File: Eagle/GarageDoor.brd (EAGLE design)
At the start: 27.4 x 31.8 mm, 30 parts, among them Q1 P-FET

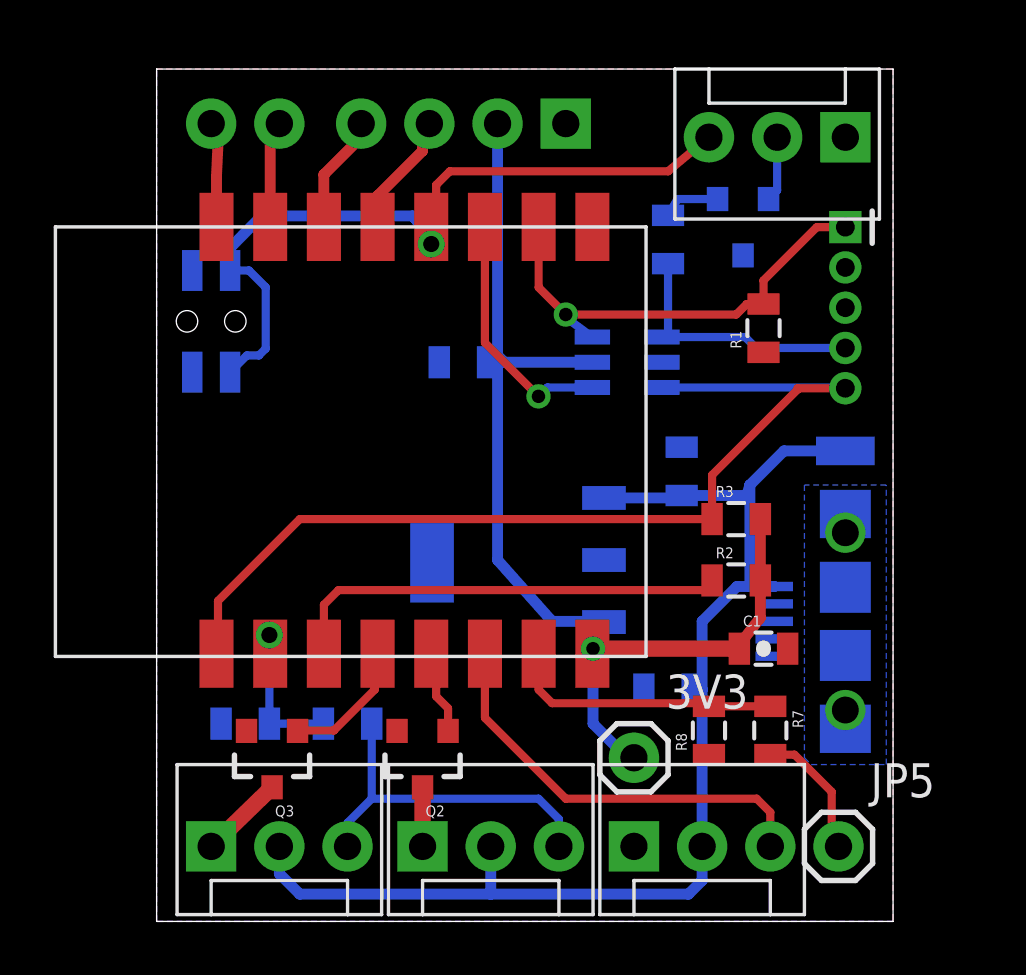
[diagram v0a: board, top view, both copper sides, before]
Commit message: Changed to positive side sensor control
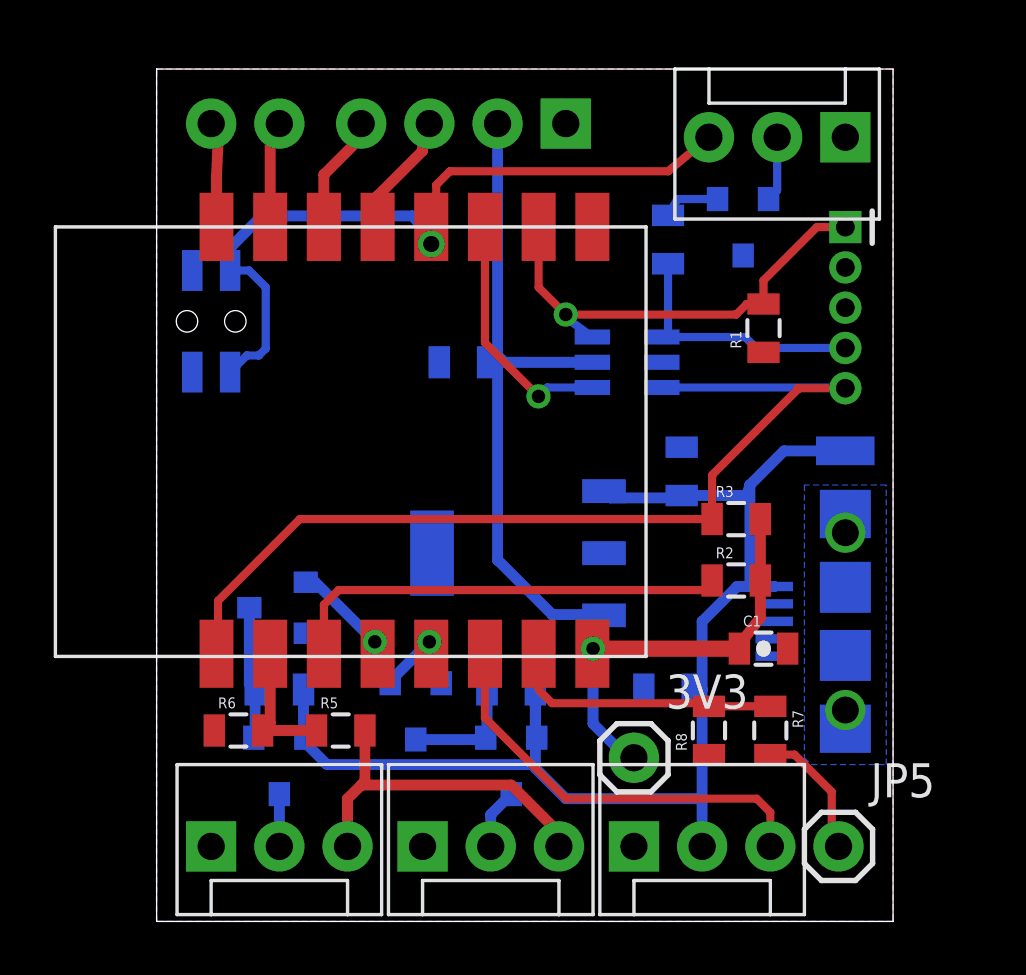
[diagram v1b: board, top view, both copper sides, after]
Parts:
- added Q4, Q5: P-FET, SparkFun-DiscreteSemi:SOT23-3
- added R10, R9: 10K, SparkFun-Resistors:0805
- moved Q3 5.59 mm to (4.55, 11.7), flipped to the bottom, turned to 270 degrees
- moved Q2 1.80 mm to (9.65, 7.87), flipped to the bottom
- moved R5 0.36 mm to (6.86, 7.11), flipped to the top, turned to 0 degrees
- moved R6 0.36 mm to (3.05, 7.11), flipped to the top, turned to 0 degrees
- moved 3V3R 0.25 mm to (13.5, 13.7)
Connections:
- new net N$12: Q2.3, Q5.1, R10.1
- new net N$13: JP3.2, Q5.3
- net +5V: now also Q4.2, Q5.2, R10.2, R9.2; no longer JP2.2, JP3.2
- net GND: now also JP2.1, JP3.1
- net N$2: now also JP2.2, Q4.3; no longer JP2.1, Q3.3
- net N$6: now also Q3.3, Q4.1, R9.1; no longer JP3.1, Q2.3
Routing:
- net N$12: track 0.00 -> 4.45 mm
- net N$6: track 2.20 -> 4.95 mm
- net N$13: track 0.00 -> 2.26 mm
- net +5V: track 46.8 -> 49.0 mm
- net IO16: track 5.64 -> 3.98 mm, vias 0 -> 1
- net N$2: track 3.16 -> 1.95 mm
- net ADC: track 6.13 -> 4.98 mm, vias 1 -> 0
- net 3V3: track 43.1 -> 42.1 mm
- net IO14: track 3.13 -> 2.69 mm, vias 0 -> 1

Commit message: Changed to NPN output
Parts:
- Q1: value P-FET -> (none)
- R10, R6, R9: value 10K -> 4K7
- R4: value 10K -> 1K
- R5: value 10K -> 5K6
- moved R4 0.76 mm to (19.1, 24.6)
- moved Q1 0.36 mm to (22.1, 25.7), turned to 90 degrees
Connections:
- net GND: now also Q1.2; no longer Q1.3
- net N$1: now also Q1.3; no longer Q1.2
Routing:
- net N$1: track 2.43 -> 3.59 mm
- net ICSPDAT: track 10.5 -> 9.89 mm
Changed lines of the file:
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@@
 <element name="." library="SparkFun-Connectors" package="1X02" value="" x="2.032" y="29.718" rot="MR180"/>
 <element name="C1" library="SparkFun-Capacitors" package="0805-CAP" value="0.1uF" x="22.606" y="10.16"/>
-<element name="Q1" library="SparkFun-DiscreteSemi" package="SOT23-3" value="P-FET" x="21.844" y="25.908" rot="MR180"/>
 <element name="U$3" library="CuriousTech" package="SMD-PAD1" value="SMD-PAD1" x="25.654" y="17.526" rot="MR180"/>
 <element name="10F320" library="Microchip_By_element14_Batch_1" package="SOT95P270X145-6N" value="PIC10F320T-I/OT" x="17.526" y="20.828" rot="MR0">
@@
 <element name="C4" library="SparkFun-Capacitors" package="0805-CAP" value="1uF" x="19.558" y="16.764" rot="MR90"/>
 <element name="JP4" library="SparkFun-Connectors" package="MOLEX-1X3" value="" x="17.78" y="2.794"/>
-<element name="R4" library="SparkFun-Resistors" package="0805" value="10K" x="19.05" y="25.4" rot="MR270"/>
+<element name="R4" library="SparkFun-Resistors" package="0805" value="1K" x="19.05" y="24.638" rot="MR270"/>
 <element name="C3" library="SparkFun-Capacitors" package="0805-CAP" value="0.1uF" x="19.05" y="8.636" rot="MR0"/>
-<element name="R5" library="SparkFun-Resistors" package="0805" value="10K" x="6.858" y="7.112"/>
-<element name="R6" library="SparkFun-Resistors" package="0805" value="10K" x="3.048" y="7.112"/>
+<element name="R5" library="SparkFun-Resistors" package="0805" value="5K6" x="6.858" y="7.112"/>
+<element name="R6" library="SparkFun-Resistors" package="0805" value="4K7" x="3.048" y="7.112"/>
 <element name="JP5" library="SparkFun-Connectors" package="1X01" value="" x="25.4" y="2.794"/>
 <element name="JP6" library="SparkFun-Connectors" package="MOLEX-1X3" value="" x="25.654" y="29.21" rot="R180"/>
@@
 <element name="3V3" library="SparkFun-Connectors" package="1X01" value="" x="17.78" y="6.096"/>
 <element name="Q4" library="SparkFun-DiscreteSemi" package="SOT23-3" value="P-FET" x="4.572" y="5.842" rot="MR180"/>
-<element name="R9" library="SparkFun-Resistors" package="0805" value="10K" x="4.572" y="8.636" rot="MR180"/>
+<element name="R9" library="SparkFun-Resistors" package="0805" value="4K7" x="4.572" y="8.636" rot="MR180"/>
 <element name="Q5" library="SparkFun-DiscreteSemi" package="SOT23-3" value="P-FET" x="13.208" y="5.842" rot="MR180"/>
-<element name="R10" library="SparkFun-Resistors" package="0805" value="10K" x="13.208" y="8.636" rot="MR180"/>
+<element name="R10" library="SparkFun-Resistors" package="0805" value="4K7" x="13.208" y="8.636" rot="MR180"/>
+<element name="Q1" library="SparkFun-DiscreteSemi" package="SOT23-3" value="" x="22.098" y="25.654" rot="MR90">
+<attribute name="PROD_ID" value="TRANS-08049" x="22.098" y="25.654" size="1.016" layer="28" ratio="18" rot="MR90" display="off"/>
+</element>
 </elements>
 <signals>
@@
 <contactref element="JP1" pad="MT2"/>
 <contactref element="C4" pad="2"/>
-<contactref element="Q1" pad="3"/>
 <contactref element="OLED" pad="1"/>
 <via x="25.654" y="7.874" extent="1-16" drill="1" shape="square"/>
@@
 <contactref element="Q3" pad="2"/>
 <contactref element="Q2" pad="2"/>
+<contactref element="Q1" pad="2"/>
 </signal>
 <signal name="TXD">
@@
 </signal>
 <signal name="N$1">
-<contactref element="Q1" pad="2"/>
 <contactref element="JP6" pad="2"/>
-<wire x1="23.114" y1="29.21" x2="23.114" y2="27.228" width="0.3048" layer="16"/>
-<wire x1="23.114" y1="27.228" x2="22.794" y2="26.908" width="0.3048" layer="16"/>
+<wire x1="23.114" y1="29.21" x2="23.114" y2="25.738" width="0.3048" layer="16"/>
+<contactref element="Q1" pad="3"/>
+<wire x1="23.114" y1="25.738" x2="23.198" y2="25.654" width="0.3048" layer="16"/>
 </signal>
 <signal name="ICSPDAT">
@@
 <contactref element="R4" pad="2"/>
 <wire x1="18.912" y1="21.8584" x2="18.8214" y2="21.7678" width="0.3048" layer="16"/>
-<wire x1="19.05" y1="24.5" x2="19.188" y2="24.5" width="0.3048" layer="16"/>
-<wire x1="19.188" y1="24.5" x2="19.05" y2="24.638" width="0.3048" layer="16"/>
-<wire x1="19.05" y1="24.638" x2="19.05" y2="21.7932" width="0.3048" layer="16"/>
+<wire x1="19.05" y1="23.738" x2="18.934" y2="23.992" width="0.3048" layer="16"/>
+<wire x1="18.934" y1="23.992" x2="19.05" y2="23.876" width="0.3048" layer="16"/>
+<wire x1="19.05" y1="23.876" x2="19.05" y2="21.7932" width="0.3048" layer="16"/>
 <wire x1="19.05" y1="21.7932" x2="18.8214" y2="21.7678" width="0.3048" layer="16"/>
 </signal>
@@
 </signal>
 <signal name="N$8">
+<contactref element="R4" pad="1"/>
 <contactref element="Q1" pad="1"/>
-<contactref element="R4" pad="1"/>
-<wire x1="20.894" y1="26.908" x2="19.404" y2="26.908" width="0.3048" layer="16"/>
-<wire x1="19.404" y1="26.908" x2="19.05" y2="26.3" width="0.3048" layer="16"/>
+<wire x1="19.05" y1="25.538" x2="19.42" y2="25.538" width="0.3048" layer="16"/>
+<wire x1="19.42" y1="25.538" x2="20.066" y2="24.892" width="0.3048" layer="16"/>
+<wire x1="20.066" y1="24.892" x2="20.91" y2="24.892" width="0.3048" layer="16"/>
+<wire x1="20.91" y1="24.892" x2="21.098" y2="24.704" width="0.3048" layer="16"/>
 </signal>
 <signal name="ANA">

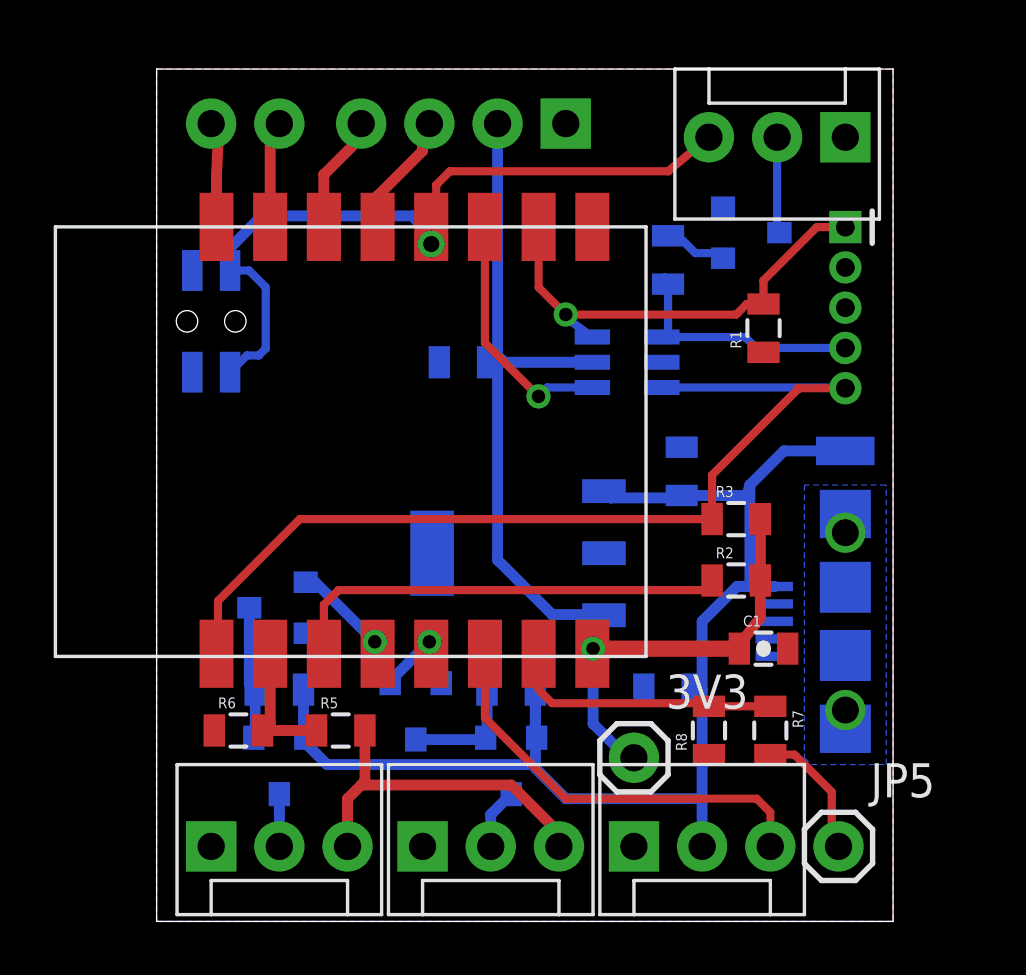
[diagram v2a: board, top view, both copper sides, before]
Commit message: Simplified, added DHT22
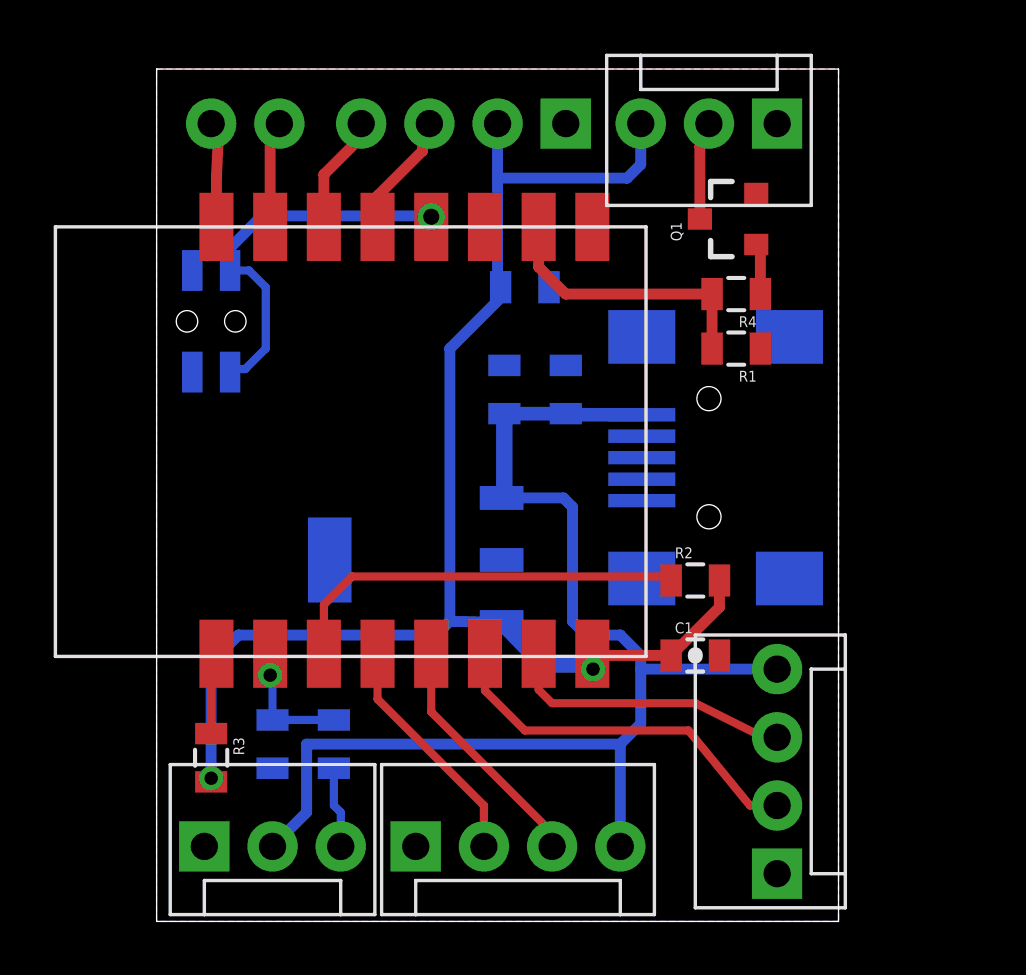
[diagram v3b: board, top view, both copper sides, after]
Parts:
- removed 10F320: PIC10F320T-I/OT, Microchip_By_element14_Batch_1:SOT95P270X145-6N
- removed 3V3, JP5: (no value), SparkFun-Connectors:1X01
- removed JP4: (no value), SparkFun-Connectors:MOLEX-1X3
- removed Q2, Q3: (no value), SparkFun-DiscreteSemi:SOT23-3
- removed Q4, Q5: P-FET, SparkFun-DiscreteSemi:SOT23-3
- removed R10, R9: 4K7, SparkFun-Resistors:0805
- removed R7, R8: 330, SparkFun-Resistors:0805
- removed U$3: SMD-PAD1, CuriousTech:SMD-PAD1
- removed U$9: PIC-ICSP-MINI, SparkFun-Connectors:PIC-ICSP-MINI
- added U$4: USB-MINIB-5PIN, SparkFun-Connectors:USB-MINIB
- JP1: value USB-MICROB -> (none); device SparkFun-Connectors:USB-MICROB -> SparkFun-Connectors:MOLEX-1X4
- JP3: device SparkFun-Connectors:MOLEX-1X3 -> SparkFun-Connectors:MOLEX-1X4
- moved R3 21.5 mm to (2.03, 6.10), turned to 270 degrees
- moved C3 12.7 mm to (13.0, 19.8), turned to 90 degrees
- moved JP1 9.74 mm to (23.1, 1.78), flipped to the top, turned to 90 degrees
- moved C4 5.29 mm to (15.2, 19.8)
- moved 3V3R 3.82 mm to (9.65, 13.5)
- moved C2 3.61 mm to (13.7, 23.6), turned to 180 degrees
- moved R4 2.84 mm to (21.6, 23.4), flipped to the top, turned to 180 degrees
- moved JP6 2.59 mm to (23.1, 29.7)
- moved C1 2.55 mm to (20.1, 9.91)
- moved R2 1.52 mm to (20.1, 12.7)
- moved R6 1.37 mm to (4.32, 6.60), flipped to the bottom, turned to 90 degrees
- moved R1 1.27 mm to (21.6, 21.3), turned to 180 degrees
- moved Q1 0.92 mm to (21.3, 26.2), flipped to the top
- moved R5 0.57 mm to (6.60, 6.60), flipped to the bottom, turned to 270 degrees
- moved JP3 0.25 mm to (9.65, 2.79)
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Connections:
- removed net ICSPDAT: 10F320.1, R4.2, U$9.4
- removed net N$12: Q2.3, Q5.1, R10.1
- removed net N$13: JP3.2, Q5.3
- removed net N$2: JP2.2, Q4.3
- removed net N$5: JP5.1, R7.2
- removed net N$6: Q3.3, Q4.1, R9.1
- net +5V: now also JP1.4, JP2.2, JP3.4, U$4.VBUS; no longer JP1.VBUS, JP4.2, Q4.2, Q5.2, R10.2, R9.2, U$3.>NAME
- net 3V3: now also JP6.3; no longer 10F320.5, 3V3.1
- net ANA: no longer JP3.3
- net GND: now also JP1.1, U$4.GND, U$4.MTN1, U$4.MTN2, U$4.MTN3, U$4.MTN4; no longer 10F320.2, JP1.GND, JP1.MT1, JP1.MT2, JP4.1, Q2.2, Q3.2, R8.1, U$9.3
- net ICSPCLK: no longer 10F320.3, U$9.5
- net IO0: no longer JP6.3
- net IO12: now also JP1.2; no longer JP4.3
- net IO13: now also JP1.3; no longer R7.1, R8.2
- net IO14: now also JP3.3; no longer Q2.1
- net IO15: now also R4.2; no longer 10F320.6, U$9.1
- net IO16: now also JP3.2; no longer Q3.1
- net IO2: no longer 10F320.4
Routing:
- net ICSPCLK: track 37.6 -> 6.72 mm
- net IO0: track 28.7 -> 15.7 mm
- net 3V3: track 42.1 -> 54.2 mm, vias 1 -> 2
- net ANA: track 13.2 -> 3.02 mm
- net ICSPDAT: track 9.89 -> 0.00 mm
- net IO2: track 9.28 -> 0.00 mm, vias 1 -> 0
- net IO14: track 2.69 -> 9.59 mm, vias 1 -> 0
- net IO15: track 17.3 -> 10.4 mm, vias 1 -> 0
- net N$5: track 5.00 -> 0.00 mm
- net N$6: track 4.95 -> 0.00 mm
- net IO16: track 3.98 -> 8.82 mm, vias 1 -> 0
- net N$12: track 4.45 -> 0.00 mm
- net N$13: track 2.26 -> 0.00 mm
- net +5V: track 49.0 -> 47.0 mm
- net N$2: track 1.95 -> 0.00 mm
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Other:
- board size 27.4 x 31.8 mm -> 25.4 x 31.8 mm
- board text removed: "WiFi Garage Door"
